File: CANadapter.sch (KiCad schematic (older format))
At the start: 27 parts, among them P1 CONN_02X06, P2 CONN_01X06, P3 CONN_01X04, U1 MCP2515, U2 TLP2361, U3 TLP2361, U4 MCP2551-I/SN, U5 7805, Y1 16MHz

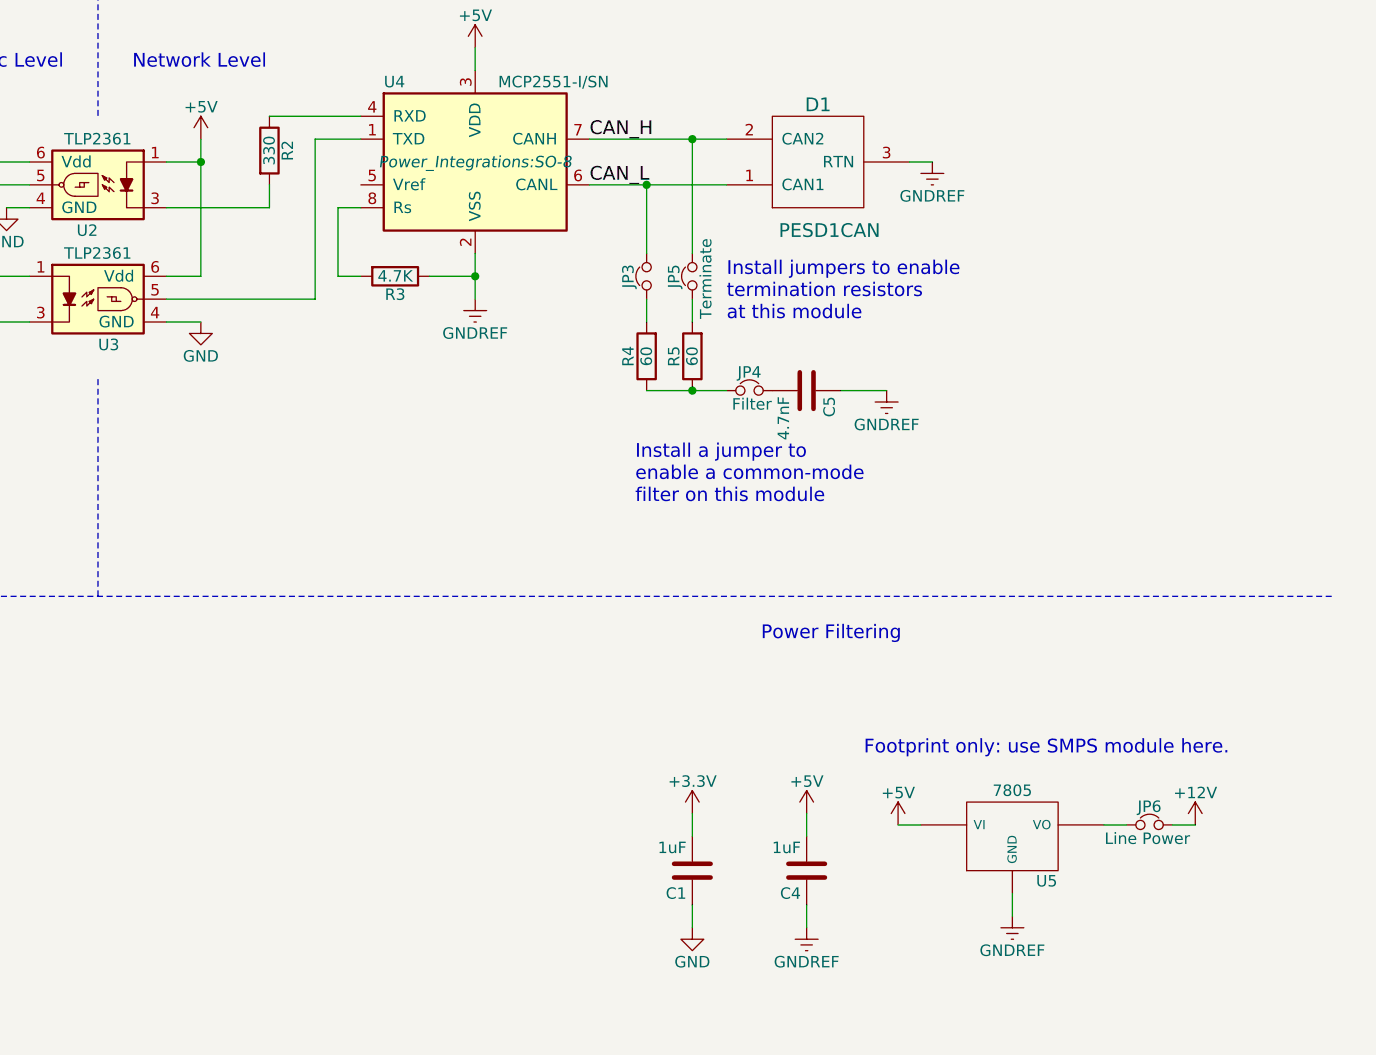
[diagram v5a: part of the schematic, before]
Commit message: corrected connectivity and pin numbering, placed parts
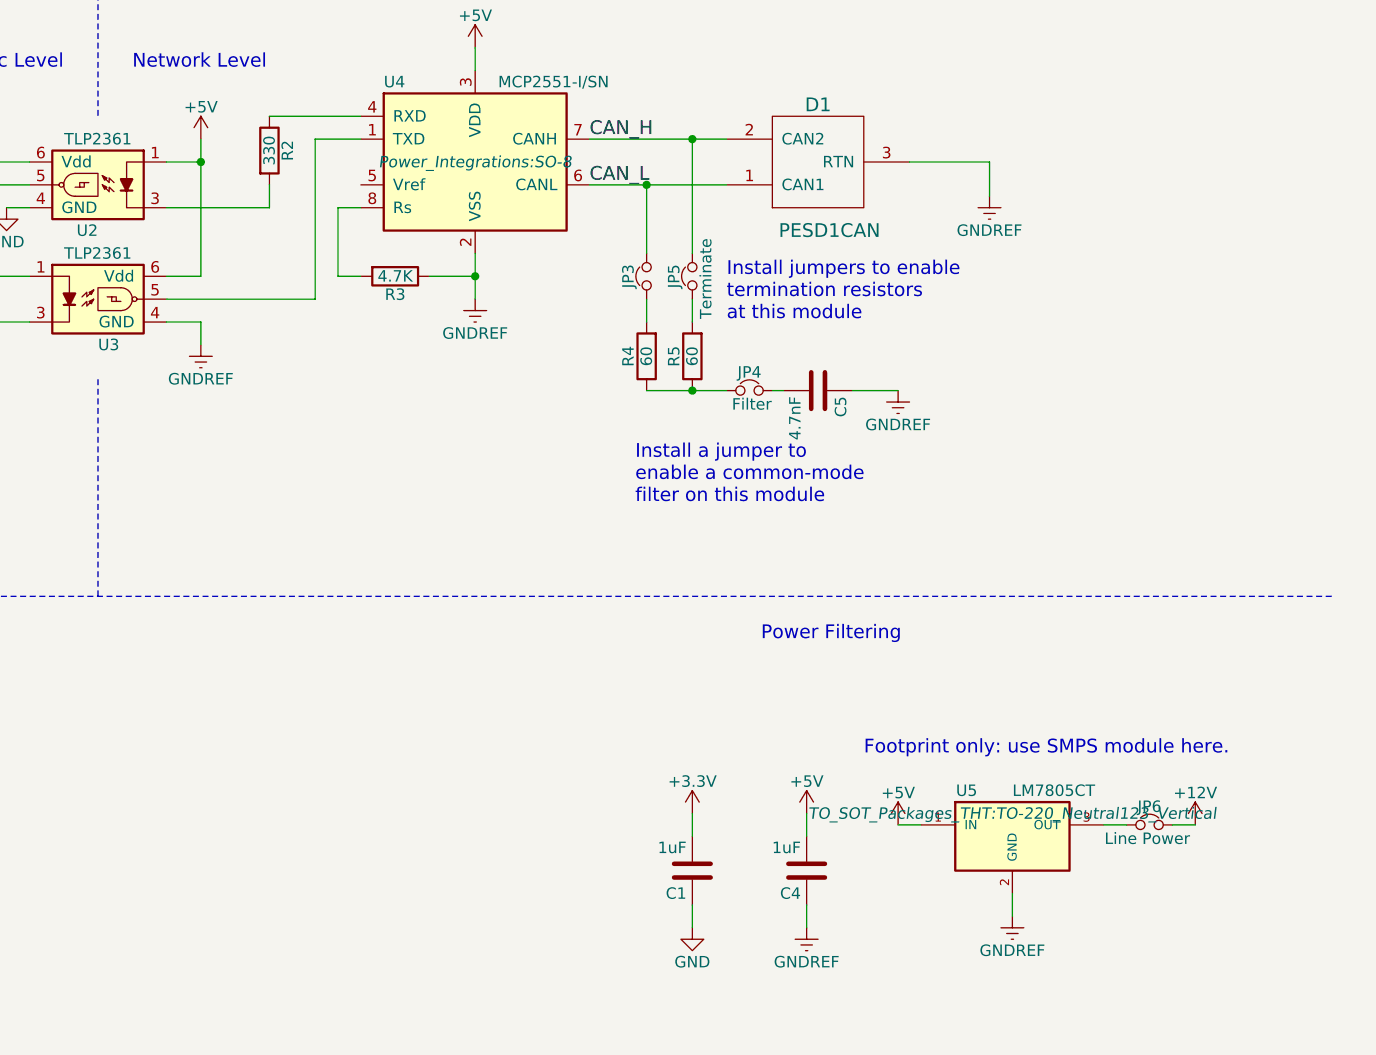
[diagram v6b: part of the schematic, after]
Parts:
- removed U5: 7805, TO_SOT_Packages_THT:TO-220_Neutral123_Vertical_LargePads, symbol 7805
- added U5: LM7805CT, TO_SOT_Packages_THT:TO-220_Neutral123_Vertical, symbol LM7805CT
- JP1, JP2, JP3, JP4, JP5, JP6: footprint (none) -> LocalLib:JumperSingleJumbo
- R1, R2, R3: footprint Resistors_SMD:R_1210_HandSoldering -> Resistors_SMD:R_0603
- R4, R5: footprint Resistors_SMD:R_1218_HandSoldering -> Resistors_SMD:R_1210
- R6: footprint Resistors_SMD:R_1206_HandSoldering -> Resistors_SMD:R_0603
- U2, U3: footprint (none) -> LocalLib:soic-5
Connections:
- net +5V: now also U5.1 (IN)
- net GND: no longer U3.4 (GND)
- net GNDREF: now also U3.4 (GND), U5.2 (GND)
- net at JP6.2: now also U5.3 (OUT)
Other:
- moved on the sheet: C5
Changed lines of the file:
@@
 $EndDescr
-$Comp
-L MCP2551-I/SN U4
-U 1 1 56AF43CB
-P 7200 1500
-F 0 "U4" H 6800 1850 50  0000 L CNN
-F 1 "MCP2551-I/SN" H 7300 1850 50  0000 L CNN
-F 2 "Power_Integrations:SO-8" H 7200 1500 50  0000 C CIN
-F 3 "" H 7200 1500 50  0000 C CNN
-	1    7200 1500
-	1    0    0    -1
-$EndComp
 $Comp
 L MCP2515 U1
@@
 F 0 "R3" V 6930 2000 50  0000 C CNN
 F 1 "4.7K" V 6850 2000 50  0000 C CNN
-F 2 "Resistors_SMD:R_1210_HandSoldering" V 6780 2000 50  0001 C CNN
+F 2 "Resistors_SMD:R_0603" V 6780 2000 50  0001 C CNN
 F 3 "" H 6850 2000 50  0000 C CNN
 	1    6850 2000
@@
 L C C5
 U 1 1 56AF5117
-P 8650 2500
-F 0 "C5" H 8675 2600 50  0000 L CNN
-F 1 "4.7nF" H 8675 2400 50  0000 L CNN
-F 2 "Capacitors_SMD:C_1206_HandSoldering" H 8688 2350 50  0001 C CNN
-F 3 "" H 8650 2500 50  0000 C CNN
-	1    8650 2500
+P 8700 2500
+F 0 "C5" H 8725 2600 50  0000 L CNN
+F 1 "4.7nF" H 8725 2400 50  0000 L CNN
+F 2 "Capacitors_SMD:C_1206_HandSoldering" H 8738 2350 50  0001 C CNN
+F 3 "" H 8700 2500 50  0000 C CNN
+	1    8700 2500
 	0    1    1    0
 $EndComp
@@
 F 0 "R4" V 8030 2350 50  0000 C CNN
 F 1 "60" V 7950 2350 50  0000 C CNN
-F 2 "Resistors_SMD:R_1218_HandSoldering" V 7880 2350 50  0001 C CNN
+F 2 "Resistors_SMD:R_1210" V 7880 2350 50  0001 C CNN
 F 3 "" H 7950 2350 50  0000 C CNN
 	1    7950 2350
@@
 F 0 "R5" V 8230 2350 50  0000 C CNN
 F 1 "60" V 8150 2350 50  0000 C CNN
-F 2 "Resistors_SMD:R_1218_HandSoldering" V 8080 2350 50  0001 C CNN
+F 2 "Resistors_SMD:R_1210" V 8080 2350 50  0001 C CNN
 F 3 "" H 8150 2350 50  0000 C CNN
 	1    8150 2350
@@
 $EndComp
 $Comp
-L PESD1CAN D1
-U 1 1 56AF57FC
-P 8700 1500
-F 0 "D1" H 8700 1250 60  0000 C CNN
-F 1 "PESD1CAN" H 8650 1800 60  0000 C CNN
-F 2 "TO_SOT_Packages_SMD:SOT-23_Handsoldering" H 8700 1500 60  0001 C CNN
-F 3 "" H 8700 1500 60  0000 C CNN
-	1    8700 1500
-	-1   0    0    1
-$EndComp
-$Comp
 L GNDREF #PWR02
 U 1 1 56AF5AF3
-P 9000 2500
-F 0 "#PWR02" H 9000 2250 50  0001 C CNN
-F 1 "GNDREF" H 9000 2350 50  0000 C CNN
-F 2 "" H 9000 2500 50  0000 C CNN
-F 3 "" H 9000 2500 50  0000 C CNN
-	1    9000 2500
+P 9050 2500
+F 0 "#PWR02" H 9050 2250 50  0001 C CNN
+F 1 "GNDREF" H 9050 2350 50  0000 C CNN
+F 2 "" H 9050 2500 50  0000 C CNN
+F 3 "" H 9050 2500 50  0000 C CNN
+	1    9050 2500
 	1    0    0    -1
 $EndComp
@@
 L GNDREF #PWR03
 U 1 1 56AF5B1D
-P 9200 1500
-F 0 "#PWR03" H 9200 1250 50  0001 C CNN
-F 1 "GNDREF" H 9200 1350 50  0000 C CNN
-F 2 "" H 9200 1500 50  0000 C CNN
-F 3 "" H 9200 1500 50  0000 C CNN
-	1    9200 1500
+P 9450 1650
+F 0 "#PWR03" H 9450 1400 50  0001 C CNN
+F 1 "GNDREF" H 9450 1500 50  0000 C CNN
+F 2 "" H 9450 1650 50  0000 C CNN
+F 3 "" H 9450 1650 50  0000 C CNN
+	1    9450 1650
 	1    0    0    -1
 $EndComp
@@
 F 0 "R2" V 6380 1450 50  0000 C CNN
 F 1 "330" V 6300 1450 50  0000 C CNN
-F 2 "Resistors_SMD:R_1210_HandSoldering" V 6230 1450 50  0001 C CNN
+F 2 "Resistors_SMD:R_0603" V 6230 1450 50  0001 C CNN
 F 3 "" H 6300 1450 50  0000 C CNN
 	1    6300 1450
@@
 F 0 "JP3" H 7950 2080 50  0000 C CNN
 F 1 "Terminate" H 7960 1940 50  0001 C CNN
-F 2 "" H 7950 2000 50  0001 C CNN
+F 2 "LocalLib:JumperSingleJumbo" H 7950 2000 50  0001 C CNN
 F 3 "" H 7950 2000 50  0000 C CNN
 	1    7950 2000
@@
 F 0 "JP5" H 8150 2080 50  0000 C CNN
 F 1 "Terminate" H 8160 1940 50  0000 C CNN
-F 2 "" H 8150 2000 50  0001 C CNN
+F 2 "LocalLib:JumperSingleJumbo" H 8150 2000 50  0001 C CNN
 F 3 "" H 8150 2000 50  0000 C CNN
 	1    8150 2000
@@
 F 0 "JP4" H 8400 2580 50  0000 C CNN
 F 1 "Filter" H 8410 2440 50  0000 C CNN
-F 2 "" H 8400 2500 50  0001 C CNN
+F 2 "LocalLib:JumperSingleJumbo" H 8400 2500 50  0001 C CNN
 F 3 "" H 8400 2500 50  0000 C CNN
 	1    8400 2500
@@
 F 0 "JP1" H 4050 1880 50  0000 C CNN
 F 1 "Use MCP2515" H 4050 1750 50  0000 C CNN
-F 2 "" H 4050 1800 50  0001 C CNN
+F 2 "LocalLib:JumperSingleJumbo" H 4050 1800 50  0001 C CNN
 F 3 "" H 4050 1800 50  0000 C CNN
 	1    4050 1800
@@
 F 0 "JP2" H 4050 1980 50  0000 C CNN
 F 1 "Use MCP2515" H 4060 1840 50  0001 C CNN
-F 2 "" H 4050 1900 50  0001 C CNN
+F 2 "LocalLib:JumperSingleJumbo" H 4050 1900 50  0001 C CNN
 F 3 "" H 4050 1900 50  0000 C CNN
 	1    4050 1900
@@
 F 0 "JP6" H 10150 4480 50  0000 C CNN
 F 1 "Line Power" H 10160 4340 50  0000 C CNN
-F 2 "" H 10150 4400 50  0001 C CNN
+F 2 "LocalLib:JumperSingleJumbo" H 10150 4400 50  0001 C CNN
 F 3 "" H 10150 4400 50  0000 C CNN
 	1    10150 4400
@@
 F 0 "R1" V 4880 2050 50  0000 C CNN
 F 1 "100" V 4800 2050 50  0000 C CNN
-F 2 "Resistors_SMD:R_1210_HandSoldering" V 4730 2050 50  0001 C CNN
+F 2 "Resistors_SMD:R_0603" V 4730 2050 50  0001 C CNN
 F 3 "" H 4800 2050 50  0000 C CNN
 	1    4800 2050
@@
 $EndComp
 $Comp
-L GND #PWR020
-U 1 1 56D68543
-P 6000 2200
-F 0 "#PWR020" H 6000 1950 50  0001 C CNN
-F 1 "GND" H 6000 2050 50  0000 C CNN
-F 2 "" H 6000 2200 50  0000 C CNN
-F 3 "" H 6000 2200 50  0000 C CNN
-	1    6000 2200
-	1    0    0    -1
-$EndComp
-$Comp
 L TLP2361 U3
 U 1 1 56D69433
@@
 F 0 "U3" H 5550 1900 50  0000 L CNN
 F 1 "TLP2361" H 5550 2300 50  0000 C CNN
-F 2 "" H 5350 1900 50  0000 L CIN
+F 2 "LocalLib:soic-5" H 5350 1900 50  0001 L CIN
 F 3 "" H 5550 2100 50  0000 L CNN
 	1    5550 2100
@@
 F 0 "U2" H 5550 1400 50  0000 L CNN
 F 1 "TLP2361" H 5550 1800 50  0000 C CNN
-F 2 "" H 5350 1400 50  0000 L CIN
+F 2 "LocalLib:soic-5" H 5350 1400 50  0001 L CIN
 F 3 "" H 5550 1600 50  0000 L CNN
 	1    5550 1600
@@
 CAN_TX
 $Comp
-L GND #PWR021
+L GND #PWR020
 U 1 1 56D69FCC
 P 1900 4800
-F 0 "#PWR021" H 1900 4550 50  0001 C CNN
+F 0 "#PWR020" H 1900 4550 50  0001 C CNN
 F 1 "GND" H 1900 4650 50  0000 C CNN
 F 2 "" H 1900 4800 50  0000 C CNN
@@
 $EndComp
 $Comp
-L +3.3V #PWR022
+L +3.3V #PWR021
 U 1 1 56D69FD3
 P 1600 5150
-F 0 "#PWR022" H 1600 5000 50  0001 C CNN
+F 0 "#PWR021" H 1600 5000 50  0001 C CNN
 F 1 "+3.3V" H 1600 5290 50  0000 C CNN
 F 2 "" H 1600 5150 50  0000 C CNN
@@
 Text Label 2950 4700 0    60   ~ 0
 SCK
-$Comp
-L 7805 U5
-U 1 1 56D69F63
-P 9550 4450
-F 0 "U5" H 9700 4254 50  0000 C CNN
-F 1 "7805" H 9550 4650 50  0000 C CNN
-F 2 "TO_SOT_Packages_THT:TO-220_Neutral123_Vertical_LargePads" H 9550 4450 50  0001 C CNN
-F 3 "" H 9550 4450 50  0000 C CNN
-	1    9550 4450
-	1    0    0    -1
-$EndComp
 Text Notes 8900 4100 0    60   ~ 0
 Footprint only: use SMPS module here.
@@
 $EndComp
 $Comp
-L GND #PWR023
+L GND #PWR022
 U 1 1 56D6B9DE
 P 3850 4800
-F 0 "#PWR023" H 3850 4550 50  0001 C CNN
+F 0 "#PWR022" H 3850 4550 50  0001 C CNN
 F 1 "GND" H 3850 4650 50  0000 C CNN
 F 2 "" H 3850 4800 50  0000 C CNN
@@
 F 0 "R6" V 1680 1750 50  0000 C CNN
 F 1 "10K" V 1600 1750 50  0000 C CNN
-F 2 "Resistors_SMD:R_1206_HandSoldering" V 1530 1750 50  0001 C CNN
+F 2 "Resistors_SMD:R_0603" V 1530 1750 50  0001 C CNN
 F 3 "" H 1600 1750 50  0000 C CNN
 	1    1600 1750
@@
 $EndComp
 $Comp
-L +3.3V #PWR024
+L +3.3V #PWR023
 U 1 1 56D6ED83
 P 1600 1500
-F 0 "#PWR024" H 1600 1350 50  0001 C CNN
+F 0 "#PWR023" H 1600 1350 50  0001 C CNN
 F 1 "+3.3V" H 1600 1640 50  0000 C CNN
 F 2 "" H 1600 1500 50  0000 C CNN
@@
 	1600 1500 1600 1600
 $Comp
-L GND #PWR025
+L GND #PWR024
 U 1 1 56D6F935
 P 3150 4800
-F 0 "#PWR025" H 3150 4550 50  0001 C CNN
+F 0 "#PWR024" H 3150 4550 50  0001 C CNN
 F 1 "GND" H 3150 4650 50  0000 C CNN
 F 2 "" H 3150 4800 50  0000 C CNN
@@
 Connection ~ 3250 5100
 $Comp
-L +3.3V #PWR026
+L +3.3V #PWR025
 U 1 1 56D6FB2D
 P 2850 5100
-F 0 "#PWR026" H 2850 4950 50  0001 C CNN
+F 0 "#PWR025" H 2850 4950 50  0001 C CNN
 F 1 "+3.3V" H 2850 5240 50  0000 C CNN
 F 2 "" H 2850 5100 50  0000 C CNN
@@
 Connection ~ 8150 2500
 Wire Wire Line
-	9000 2500 8800 2500
-Wire Wire Line
-	9200 1500 9100 1500
+	9050 2500 8850 2500
 Wire Wire Line
 	1600 6400 1800 6400
 Wire Wire Line
 	1800 6400 1800 6100
+Wire Wire Line
+	8550 2500 8500 2500
+Wire Wire Line
+	9100 1500 9450 1500
+Wire Wire Line
+	9450 1500 9450 1650
+$Comp
+L PESD1CAN D1
+U 1 1 56EF8D48
+P 8700 1500
+F 0 "D1" H 8700 1250 60  0000 C CNN
+F 1 "PESD1CAN" H 8650 1800 60  0000 C CNN
+F 2 "TO_SOT_Packages_SMD:SOT-23_Handsoldering" H 8700 1500 60  0001 C CNN
+F 3 "" H 8700 1500 60  0000 C CNN
+	1    8700 1500
+	-1   0    0    1
+$EndComp
+$Comp
+L MCP2551-I/SN U4
+U 1 1 56EF927A
+P 7200 1500
+F 0 "U4" H 6800 1850 50  0000 L CNN
+F 1 "MCP2551-I/SN" H 7300 1850 50  0000 L CNN
+F 2 "Power_Integrations:SO-8" H 7200 1500 50  0000 C CIN
+F 3 "" H 7200 1500 50  0000 C CNN
+	1    7200 1500
+	1    0    0    -1
+$EndComp
+$Comp
+L GNDREF #PWR026
+U 1 1 56EF979F
+P 6000 2300
+F 0 "#PWR026" H 6000 2050 50  0001 C CNN
+F 1 "GNDREF" H 6000 2150 50  0000 C CNN
+F 2 "" H 6000 2300 50  0000 C CNN
+F 3 "" H 6000 2300 50  0000 C CNN
+	1    6000 2300
+	1    0    0    -1
+$EndComp
+Wire Wire Line
+	6000 2200 6000 2300
+$Comp
+L LM7805CT U5
+U 1 1 56EF9EFC
+P 9550 4450
+F 0 "U5" H 9350 4650 50  0000 C CNN
+F 1 "LM7805CT" H 9550 4650 50  0000 L CNN
+F 2 "TO_SOT_Packages_THT:TO-220_Neutral123_Vertical" H 9550 4550 50  0000 C CIN
+F 3 "" H 9550 4450 50  0000 C CNN
+	1    9550 4450
+	1    0    0    -1
+$EndComp
 $EndSCHEMATC

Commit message: substituted footprints, layout first pass complete
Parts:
- removed R6: 10K, Resistors_SMD:R_0603, symbol R
- added P4: CONN_01X06, Pin_Headers:Pin_Header_Straight_1x06, symbol CONN_01X06
- C1, C4: footprint Capacitors_SMD:C_1206_HandSoldering -> Capacitors_SMD:C_1210
- C2, C3: footprint Capacitors_SMD:C_0603_HandSoldering -> Capacitors_SMD:C_0603
- C5: footprint Capacitors_SMD:C_1206_HandSoldering -> Capacitors_SMD:C_1206
- Y1: footprint Crystals:Crystal_HC49-SD_SMD -> Crystals:Crystal_SMD_5032_2Pads
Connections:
- net +3V3: now also P4.6 (P6)
- net CAN_RX: now also P4.3 (P3)
- net CAN_TX: now also P4.2 (P2)
- net GND: now also P4.5 (P5)
- net at P2.1 (P1): now also P4.1 (P1)
- net at P2.4 (P4): now also P4.4 (P4)
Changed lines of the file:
@@
 F 0 "C5" H 8725 2600 50  0000 L CNN
 F 1 "4.7nF" H 8725 2400 50  0000 L CNN
-F 2 "Capacitors_SMD:C_1206_HandSoldering" H 8738 2350 50  0001 C CNN
+F 2 "Capacitors_SMD:C_1206" H 8738 2350 50  0001 C CNN
 F 3 "" H 8700 2500 50  0000 C CNN
 	1    8700 2500
@@
 F 0 "Y1" H 3450 1500 50  0000 C CNN
 F 1 "16MHz" H 3450 1300 50  0000 C CNN
-F 2 "Crystals:Crystal_HC49-SD_SMD" H 3450 1400 50  0001 C CNN
+F 2 "Crystals:Crystal_SMD_5032_2Pads" H 3450 1400 50  0001 C CNN
 F 3 "" H 3450 1400 50  0000 C CNN
 	1    3450 1400
@@
 F 0 "C2" H 3825 1300 50  0000 L CNN
 F 1 "18pF" H 3825 1100 50  0000 L CNN
-F 2 "Capacitors_SMD:C_0603_HandSoldering" H 3838 1050 50  0001 C CNN
+F 2 "Capacitors_SMD:C_0603" H 3838 1050 50  0001 C CNN
 F 3 "" H 3800 1200 50  0000 C CNN
 	1    3800 1200
@@
 F 0 "C3" H 3825 1600 50  0000 L CNN
 F 1 "18pF" H 3825 1400 50  0000 L CNN
-F 2 "Capacitors_SMD:C_0603_HandSoldering" H 3838 1350 50  0001 C CNN
+F 2 "Capacitors_SMD:C_0603" H 3838 1350 50  0001 C CNN
 F 3 "" H 3800 1500 50  0000 C CNN
 	1    3800 1500
@@
 F 0 "C1" H 8175 4700 50  0000 L CNN
 F 1 "1uF" H 8175 4500 50  0000 L CNN
-F 2 "Capacitors_SMD:C_1206_HandSoldering" H 8188 4450 50  0001 C CNN
+F 2 "Capacitors_SMD:C_1210" H 8188 4450 50  0001 C CNN
 F 3 "" H 8150 4600 50  0000 C CNN
 	1    8150 4600
@@
 F 0 "C4" H 8675 4700 50  0000 L CNN
 F 1 "1uF" H 8675 4500 50  0000 L CNN
-F 2 "Capacitors_SMD:C_1206_HandSoldering" H 8688 4450 50  0001 C CNN
+F 2 "Capacitors_SMD:C_1210" H 8688 4450 50  0001 C CNN
 F 3 "" H 8650 4600 50  0000 C CNN
 	1    8650 4600
@@
 	5850 2200 6000 2200
 Wire Wire Line
-	1700 4800 1900 4800
+	1250 4800 1900 4800
 Wire Wire Line
 	1600 5150 1800 5150
 Wire Wire Line
-	1700 4900 1800 4900
+	1250 4900 1800 4900
 Wire Wire Line
 	1800 4900 1800 5150
 Wire Wire Line
-	2200 4600 1700 4600
-Wire Wire Line
-	2200 4500 1700 4500
+	1250 4600 2200 4600
+Wire Wire Line
+	1250 4500 2200 4500
 Wire Notes Line
 	5550 600  5550 1300
@@
 	2850 5100 3750 5100
 Wire Wire Line
-	1600 1900 2100 1900
+	1800 1900 2100 1900
 Wire Wire Line
 	3200 2100 3450 2100
@@
 	1800 1700 2100 1700
 $Comp
-L R R6
-U 1 1 56D6EC59
-P 1600 1750
-F 0 "R6" V 1680 1750 50  0000 C CNN
-F 1 "10K" V 1600 1750 50  0000 C CNN
-F 2 "Resistors_SMD:R_0603" V 1530 1750 50  0001 C CNN
-F 3 "" H 1600 1750 50  0000 C CNN
-	1    1600 1750
-	-1   0    0    1
-$EndComp
-$Comp
-L +3.3V #PWR023
-U 1 1 56D6ED83
-P 1600 1500
-F 0 "#PWR023" H 1600 1350 50  0001 C CNN
-F 1 "+3.3V" H 1600 1640 50  0000 C CNN
-F 2 "" H 1600 1500 50  0000 C CNN
-F 3 "" H 1600 1500 50  0000 C CNN
-	1    1600 1500
-	1    0    0    -1
-$EndComp
-Wire Wire Line
-	1600 1500 1600 1600
-$Comp
-L GND #PWR024
+L GND #PWR023
 U 1 1 56D6F935
 P 3150 4800
-F 0 "#PWR024" H 3150 4550 50  0001 C CNN
+F 0 "#PWR023" H 3150 4550 50  0001 C CNN
 F 1 "GND" H 3150 4650 50  0000 C CNN
 F 2 "" H 3150 4800 50  0000 C CNN
@@
 Connection ~ 3250 5100
 $Comp
-L +3.3V #PWR025
+L +3.3V #PWR024
 U 1 1 56D6FB2D
 P 2850 5100
-F 0 "#PWR025" H 2850 4950 50  0001 C CNN
+F 0 "#PWR024" H 2850 4950 50  0001 C CNN
 F 1 "+3.3V" H 2850 5240 50  0000 C CNN
 F 2 "" H 2850 5100 50  0000 C CNN
@@
 $EndComp
 $Comp
-L GNDREF #PWR026
+L GNDREF #PWR025
 U 1 1 56EF979F
 P 6000 2300
-F 0 "#PWR026" H 6000 2050 50  0001 C CNN
+F 0 "#PWR025" H 6000 2050 50  0001 C CNN
 F 1 "GNDREF" H 6000 2150 50  0000 C CNN
 F 2 "" H 6000 2300 50  0000 C CNN
@@
 	1    0    0    -1
 $EndComp
+$Comp
+L CONN_01X06 P4
+U 1 1 57409659
+P 1050 4650
+F 0 "P4" H 1050 5000 50  0000 C CNN
+F 1 "CONN_01X06" V 1150 4650 50  0000 C CNN
+F 2 "Pin_Headers:Pin_Header_Straight_1x06" H 1050 4650 50  0001 C CNN
+F 3 "" H 1050 4650 50  0000 C CNN
+	1    1050 4650
+	-1   0    0    -1
+$EndComp
+Connection ~ 1700 4500
+Connection ~ 1700 4600
+Connection ~ 1700 4800
+Connection ~ 1700 4900
+Wire Wire Line
+	1700 4700 1250 4700
+Wire Wire Line
+	1700 4400 1250 4400
 $EndSCHEMATC
